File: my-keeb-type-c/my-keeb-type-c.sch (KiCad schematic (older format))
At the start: 108 parts, among them SW1 SW_Push, U1 ATmega32U4-AU, Y1 16MHz

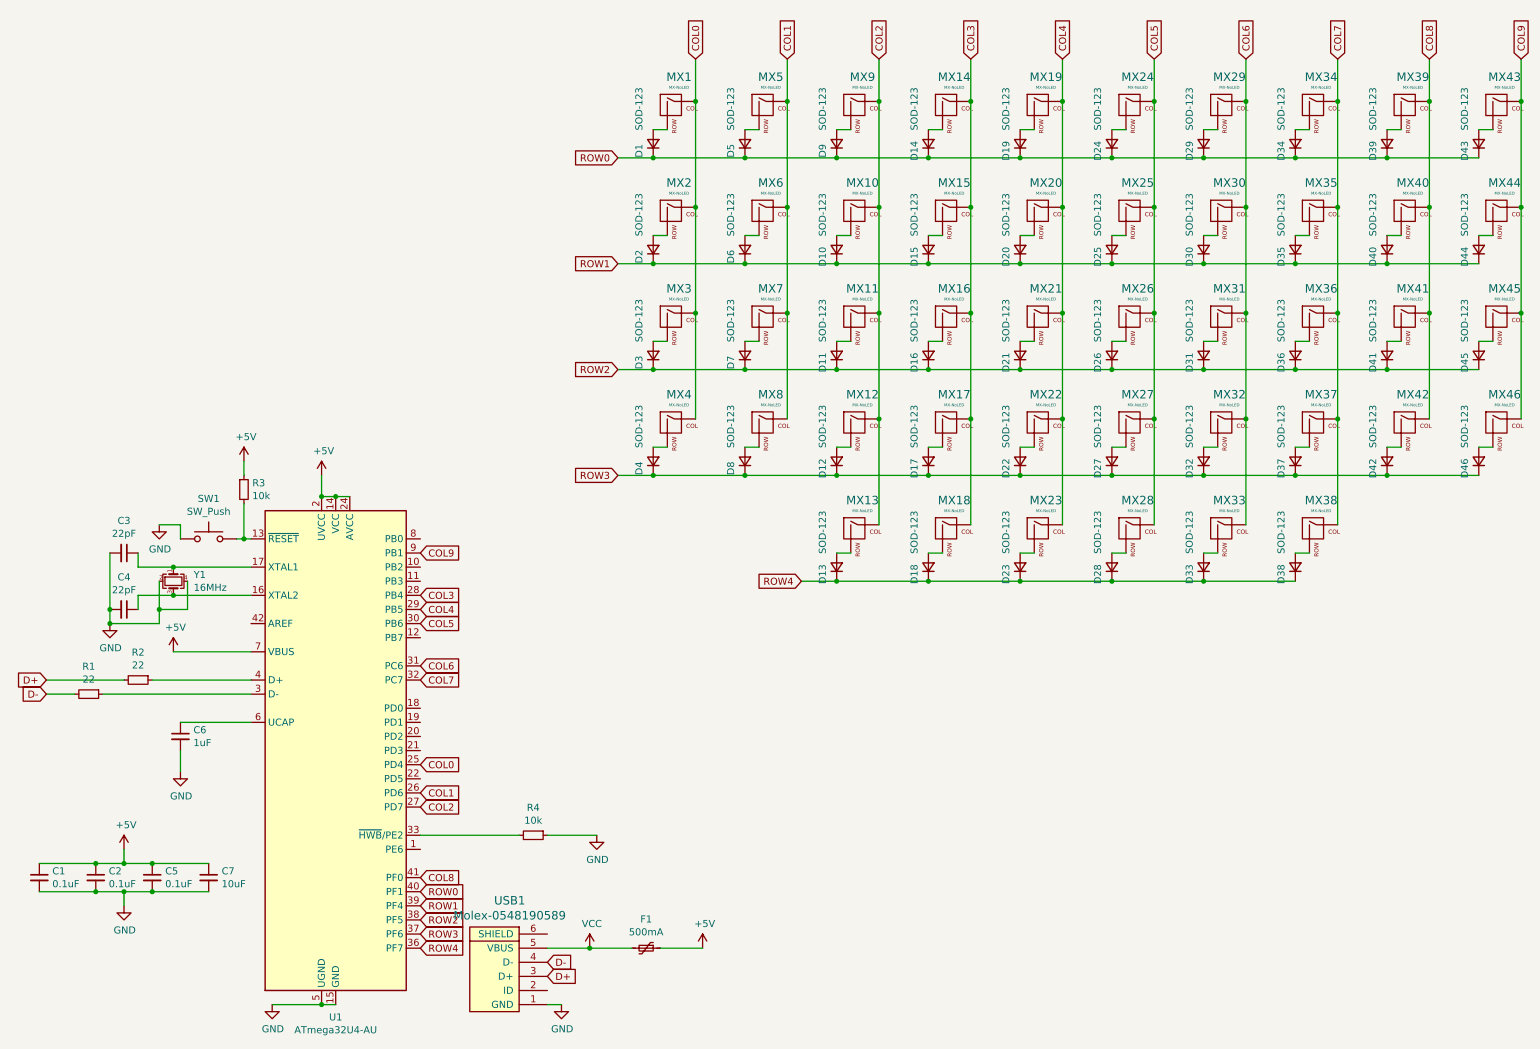
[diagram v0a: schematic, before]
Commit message: Finished type c model
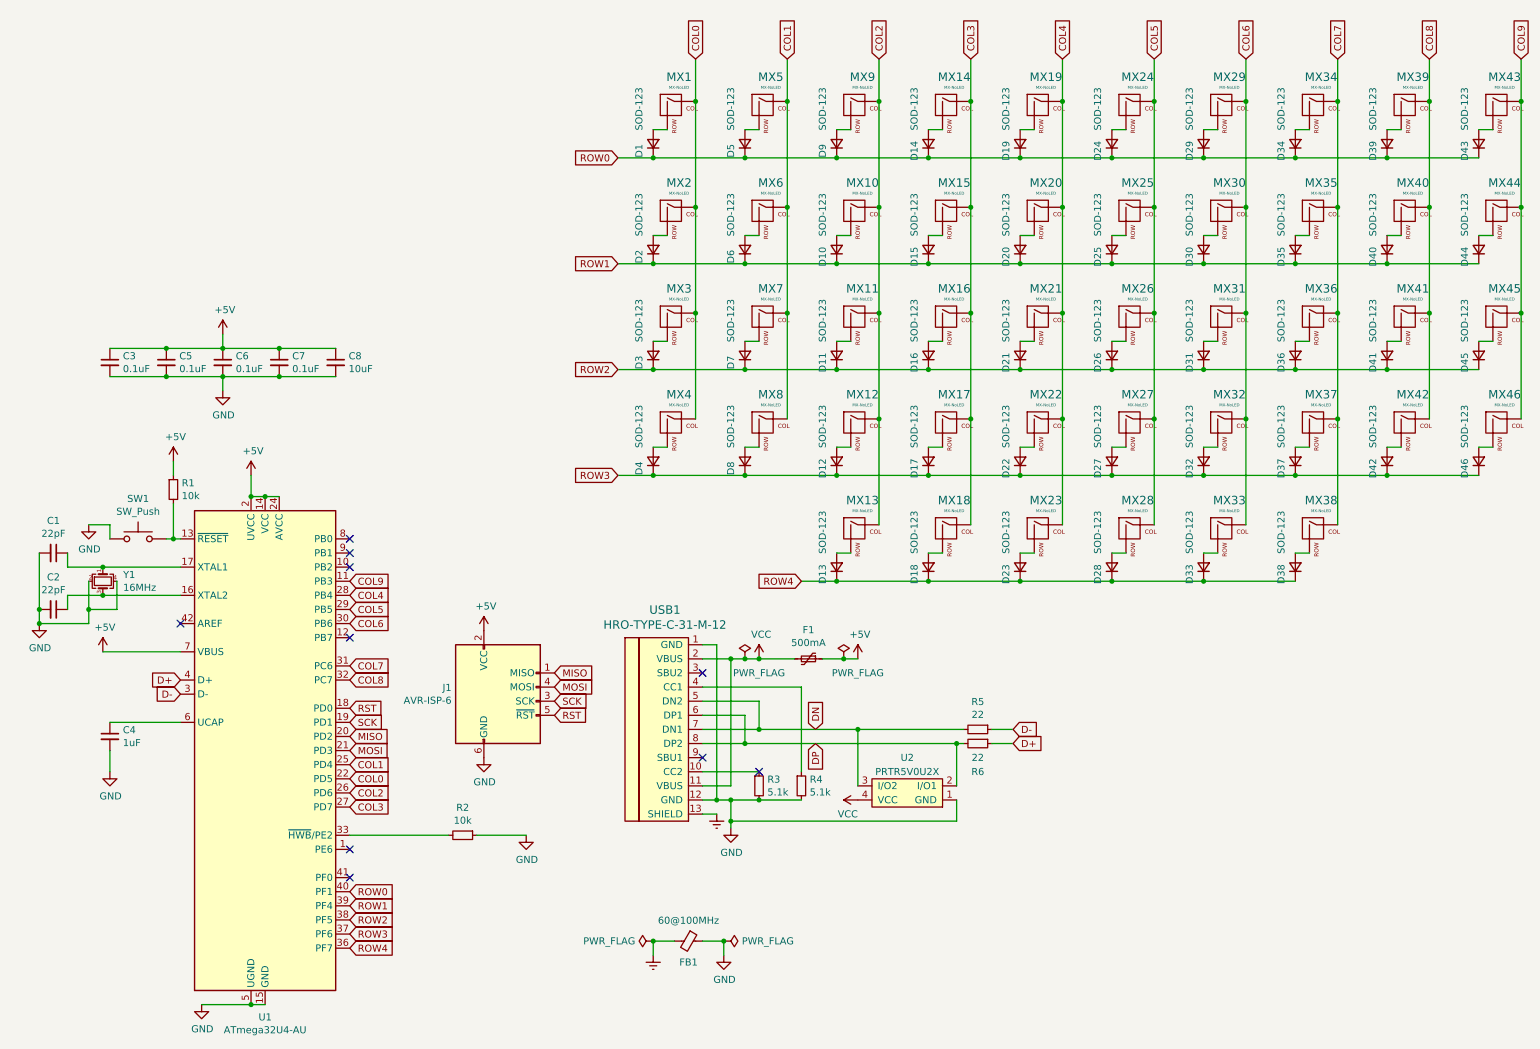
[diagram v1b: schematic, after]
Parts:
- removed USB1: Molex-0548190589, random-keyboard-parts:Molex-0548190589, symbol random-keyboard-parts:Molex-0548190589
- added C3: 0.1uF, Capacitor_SMD:C_0805_2012Metric_Pad1.18x1.45mm_HandSolder, symbol Device:C_Small
- added FB1: 60@100MHz, Inductor_SMD:L_0805_2012Metric_Pad1.15x1.40mm_HandSolder, symbol Device:Ferrite_Bead_Small
- added J1: AVR-ISP-6, random-keyboard-parts:Reset_Pretty-Mask, symbol Connector:AVR-ISP-6
- added R3, R4: 5.1k, Resistor_SMD:R_0805_2012Metric_Pad1.20x1.40mm_HandSolder, symbol Device:R_Small
- added U2: PRTR5V0U2X, random-keyboard-parts:SOT143B, symbol keebio:PRTR5V0U2X
- added USB1: HRO-TYPE-C-31-M-12, Type-C:HRO-TYPE-C-31-M-12-HandSoldering, symbol Type-C:HRO-TYPE-C-31-M-12
- C1: renamed from C3; footprint Capacitor_SMD:C_0805_2012Metric -> Capacitor_SMD:C_0805_2012Metric_Pad1.18x1.45mm_HandSolder
- C2: renamed from C4; footprint Capacitor_SMD:C_0805_2012Metric -> Capacitor_SMD:C_0805_2012Metric_Pad1.18x1.45mm_HandSolder
- C4: renamed from C6; footprint Capacitor_SMD:C_0805_2012Metric -> Capacitor_SMD:C_0805_2012Metric_Pad1.18x1.45mm_HandSolder
- C5: renamed from C1; footprint Capacitor_SMD:C_0805_2012Metric -> Capacitor_SMD:C_0805_2012Metric_Pad1.18x1.45mm_HandSolder
- C6: renamed from C2; footprint Capacitor_SMD:C_0805_2012Metric -> Capacitor_SMD:C_0805_2012Metric_Pad1.18x1.45mm_HandSolder
- C7: renamed from C5; footprint Capacitor_SMD:C_0805_2012Metric -> Capacitor_SMD:C_0805_2012Metric_Pad1.18x1.45mm_HandSolder
- C8: renamed from C7; footprint Capacitor_SMD:C_0805_2012Metric -> Capacitor_SMD:C_0805_2012Metric_Pad1.18x1.45mm_HandSolder
- F1: footprint Fuse:Fuse_1206_3216Metric -> Fuse:Fuse_1206_3216Metric_Pad1.42x1.75mm_HandSolder
- R1: renamed from R3; footprint Resistor_SMD:R_0805_2012Metric -> Resistor_SMD:R_0805_2012Metric_Pad1.20x1.40mm_HandSolder
- R2: renamed from R4; footprint Resistor_SMD:R_0805_2012Metric -> Resistor_SMD:R_0805_2012Metric_Pad1.20x1.40mm_HandSolder
- R5: renamed from R1; footprint Resistor_SMD:R_0805_2012Metric -> Resistor_SMD:R_0805_2012Metric_Pad1.20x1.40mm_HandSolder
- R6: renamed from R2; footprint Resistor_SMD:R_0805_2012Metric -> Resistor_SMD:R_0805_2012Metric_Pad1.20x1.40mm_HandSolder
- SW1: footprint random-keyboard-parts:SKQG-1155865 -> Button_Switch_SMD:SW_SPST_SKQG_WithStem
- Y1: footprint Crystal:Crystal_SMD_3225-4Pin_3.2x2.5mm -> Crystal:Crystal_SMD_3225-4Pin_3.2x2.5mm_HandSoldering
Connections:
- net +5V: now also C3.1, J1.2 (VCC)
- net COL0: now also U1.22 (PD5); no longer U1.25 (PD4)
- net COL1: now also U1.25 (PD4); no longer U1.26 (PD6)
- net COL2: now also U1.26 (PD6); no longer U1.27 (PD7)
- net COL3: now also U1.27 (PD7); no longer U1.28 (PB4)
- net COL4: now also U1.28 (PB4); no longer U1.29 (PB5)
- net COL5: now also U1.29 (PB5); no longer U1.30 (PB6)
- net COL6: now also U1.30 (PB6); no longer U1.31 (PC6)
- net COL7: now also U1.31 (PC6); no longer U1.32 (PC7)
- net COL8: now also U1.32 (PC7); no longer U1.41 (PF0)
- net COL9: now also U1.11 (PB3); no longer U1.9 (PB1)
- net D+: now also R6.1, U1.4 (D+); no longer R6.2
- net D-: now also R5.1, U1.3 (D-); no longer R5.2
- net GND: now also C3.2, FB1.1, J1.6 (GND), R3.2, R4.2, U2.1 (GND), USB1.1 (GND), USB1.12 (GND)
- net VCC: now also U2.4 (VCC), USB1.11 (VBUS), USB1.2 (VBUS)
- net RST: now reaches U1.18 (PD0)
- net RST: now also J1.5 (~RST)
- net SCK: now reaches U1.19 (PD1)
- net SCK: now also J1.3 (SCK)
- net MISO: now reaches U1.20 (PD2)
- net MISO: now also J1.1 (MISO)
- net MOSI: now reaches U1.21 (PD3)
- net MOSI: now also J1.4 (MOSI)
- new net: R3.1, USB1.10 (CC2)
- new net: R4.1, USB1.4 (CC1)
- new net DN: R5.2, U2.3 (I/O2), USB1.5 (DN2), USB1.7 (DN1)
- new net DP: R6.2, U2.2 (I/O1), USB1.6 (DP1), USB1.8 (DP2)
- new net Earth: FB1.2, USB1.13 (SHIELD)
- no-connect marks 0 -> 10
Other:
- moved on the sheet: C1, C2, C4, C5, C6, C7, C8, R1, R2, R5, R6, SW1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

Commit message: Created some plateless gasket mount pcbs
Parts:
- C1, C2: LCSC (none) -> C1804
- C3, C5, C6, C7: LCSC (none) -> C49678
- C4: LCSC (none) -> C28323
- C8: LCSC (none) -> C440198
- D1, D10, D11, D12, D13, D14, D15, D16, D17, D18, D19, D2, D20, D21, D22, D23, D24, D25, D26, D27, D28, D29, D3, D30, D31, D32, D33, D34, D35, D36, D37, D38, D39, D4, D40, D41, D42, D43, D44, D45, D46, D5, D6, D7, D8, D9: LCSC (none) -> C81598
- F1: LCSC (none) -> C70069
- FB1: LCSC (none) -> C18305
- R1, R2: LCSC (none) -> C17414
- R3, R4: LCSC (none) -> C27834
- R5, R6: LCSC (none) -> C17561
- SW1: LCSC (none) -> C318884
- U1: LCSC (none) -> C44854
- U2: LCSC (none) -> C12333
- USB1: LCSC (none) -> C165948
- Y1: LCSC (none) -> C13738
